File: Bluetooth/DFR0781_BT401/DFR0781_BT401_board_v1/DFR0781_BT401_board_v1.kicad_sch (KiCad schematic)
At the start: 8 parts, among them J1 PINHD_1x8_Female, J2 PINHD_1x6_Male

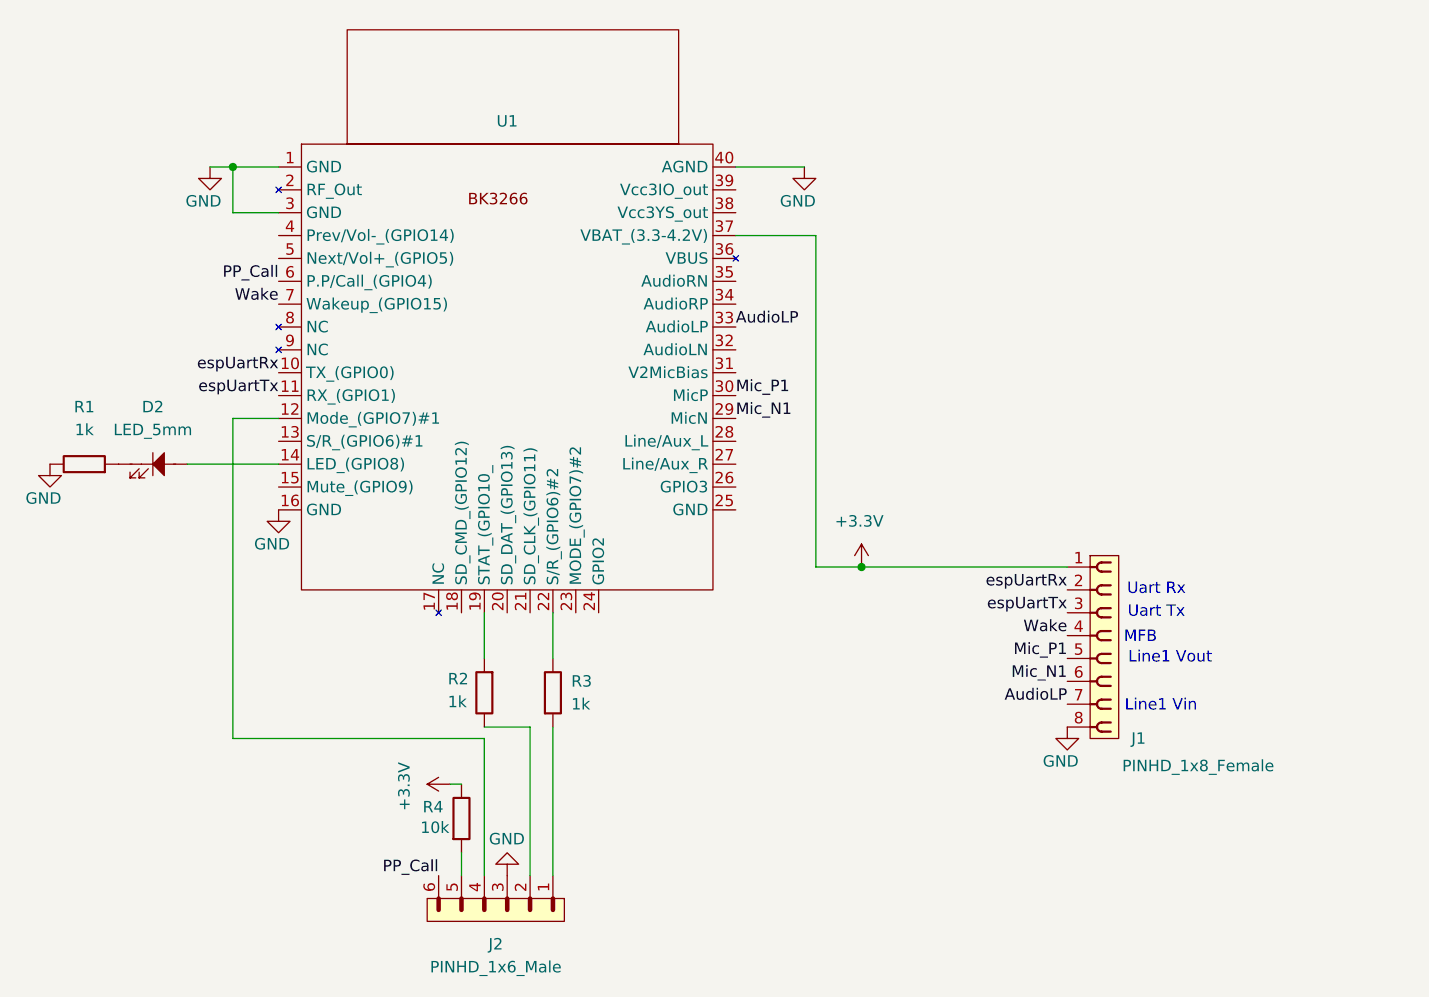
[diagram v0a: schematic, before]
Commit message: BT401 notes: measured round-pad connections (GND, SGND via 10 ohm, 5V=VCC, TX, RX)
Co-Authored-By: Claude Opus 5.5 <noreply@anthropic.com>
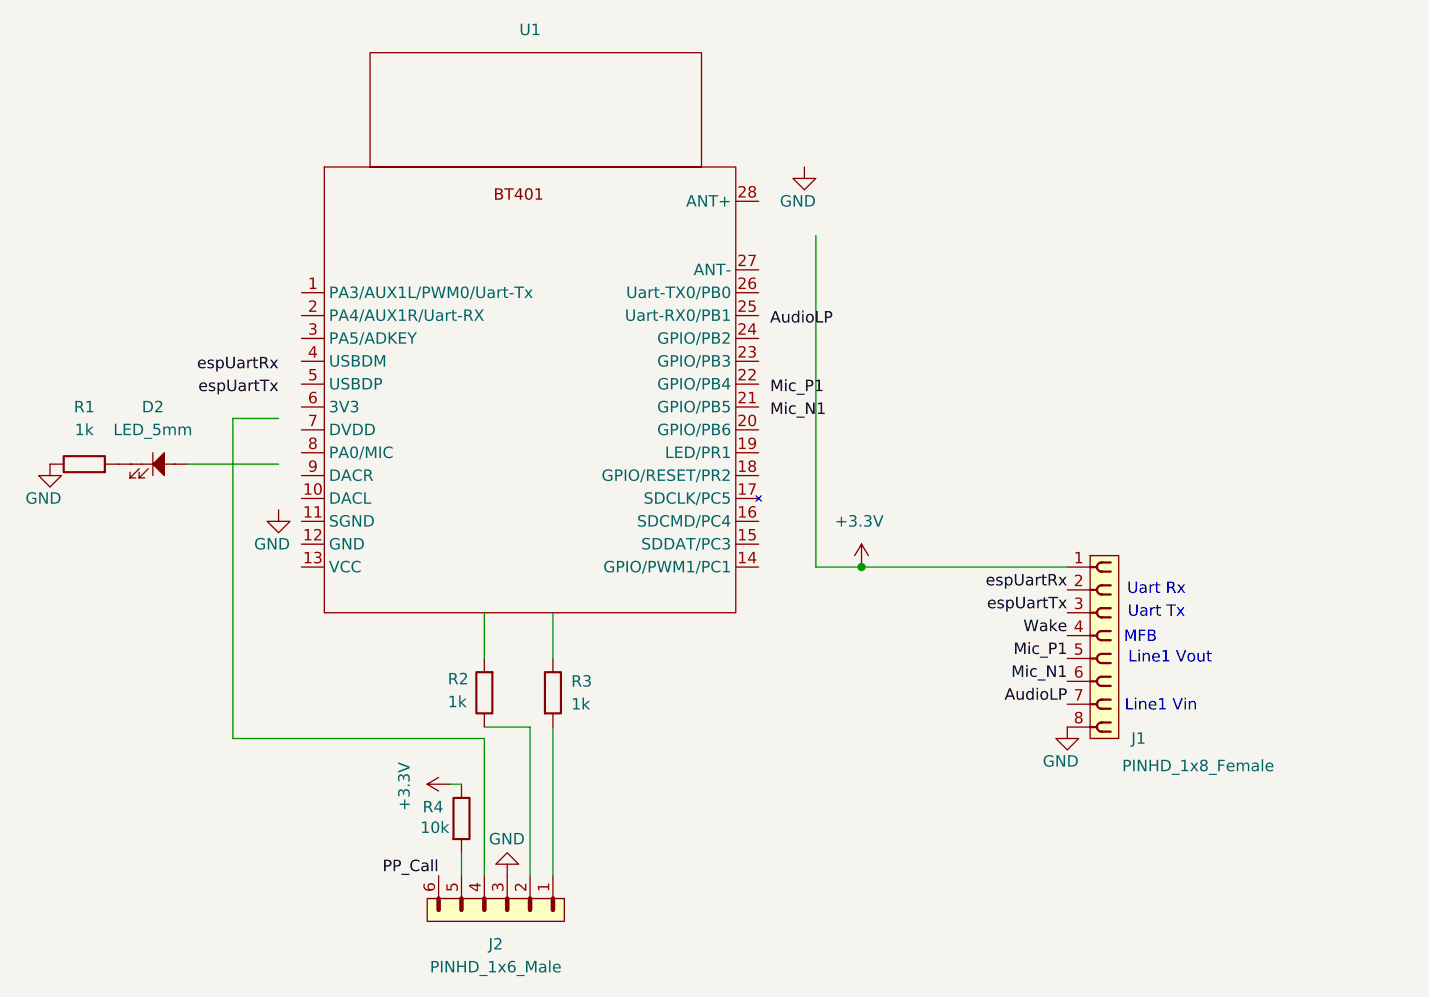
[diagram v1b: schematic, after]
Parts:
- removed U1: (no value), Custom:BK3266SR, symbol Custom:BK3266SR
- added U1: (no value), Custom:DFR0781_BT401, symbol Custom:DFR0781_BT401_Bluetooth_Module

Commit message: BT401 adapter: new symbol and footprint (round pads joined to edge pads)
Co-Authored-By: Claude Opus 5.5 <noreply@anthropic.com>
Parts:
- U1: footprint Custom:DFR0781_BT401 -> Custom:DFR0781_BT401_new
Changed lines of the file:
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@@
 			)
 		)
-		(property "Footprint" "Custom:DFR0781_BT401"
+		(property "Footprint" "Custom:DFR0781_BT401_new"
 			(at 94.742 74.168 0)
 			(hide yes)
@@
 			)
 		)
-		(property "Datasheet" ""
+		(property "Datasheet" "https://github.com/DFRobot/DFRobot_BT401"
 			(at 77.47 72.39 0)
 			(hide yes)

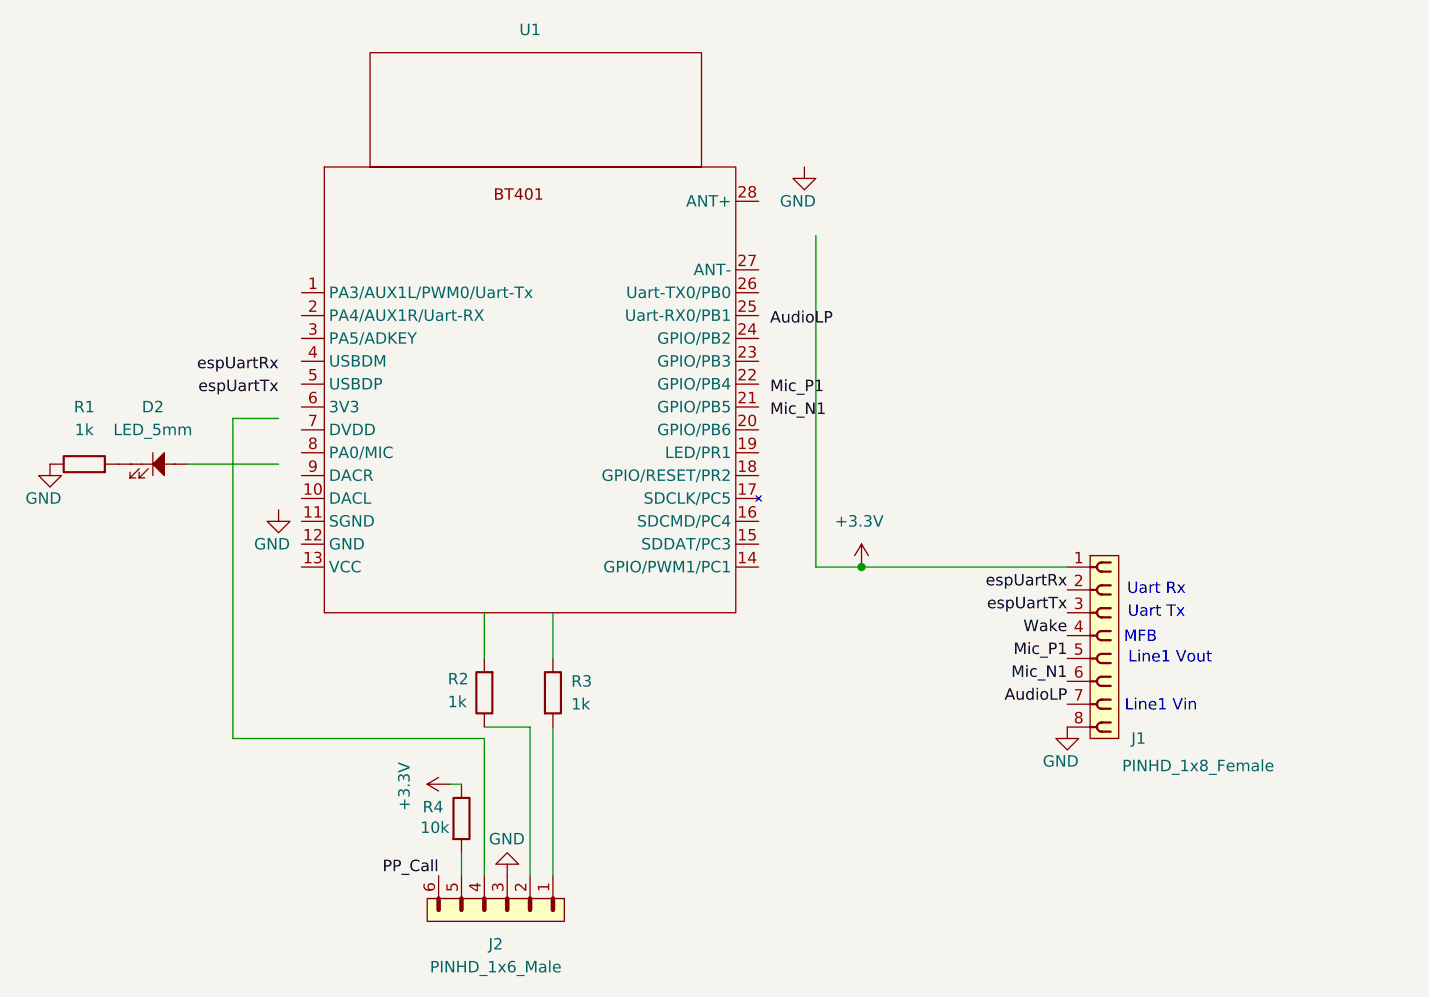
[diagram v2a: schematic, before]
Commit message: BT401: Bluetooth on/off switch puts the module in idle mode (7 mA); re-send DAC off after a module restart
Co-Authored-By: Claude Opus 5.5 <noreply@anthropic.com>
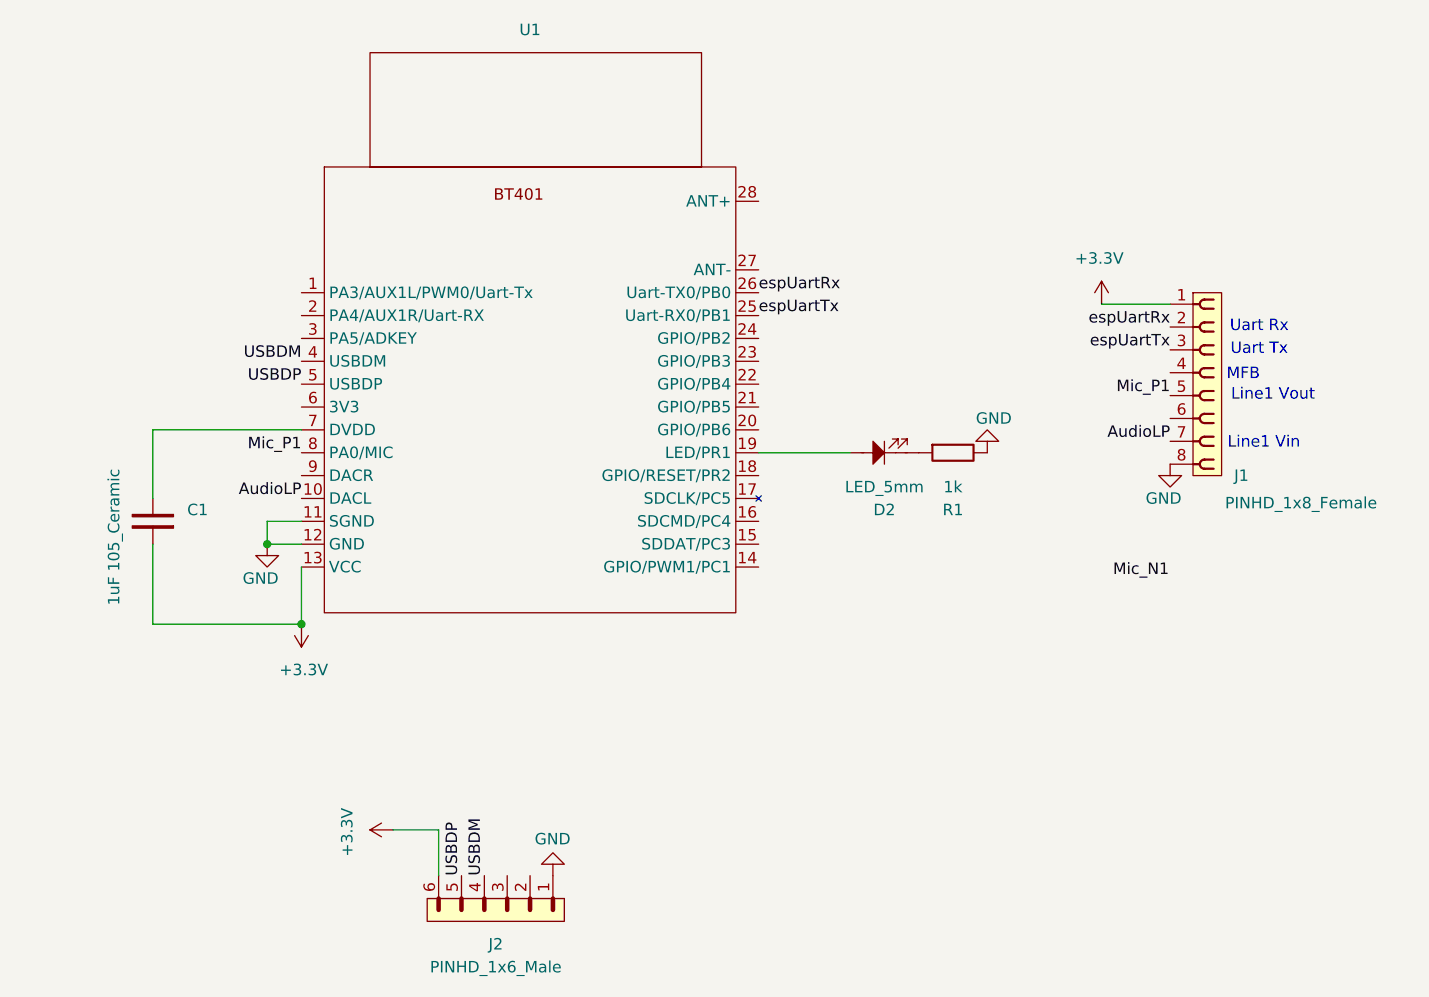
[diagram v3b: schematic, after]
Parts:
- removed R2, R3: 1k, Resistor_THT:R_Axial_DIN0207_L6.3mm_D2.5mm_P10.16mm_Horizontal, symbol PCM_SL_Resistors:1k
- removed R4: 10k, Resistor_THT:R_Axial_DIN0207_L6.3mm_D2.5mm_P10.16mm_Horizontal, symbol PCM_SL_Resistors:1k
- added C1: 1uF 105_Ceramic, Capacitor_THT:C_Disc_D5.0mm_W2.5mm_P2.50mm, symbol PCM_SL_Capacitors:104_Ceramic
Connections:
- net PP_Call is gone; now on net +3.3V: J2.6
- net +3.3V: now also U1.13 (VCC), C1.2
- net AudioLP: now also U1.10 (DACL)
- net GND: now also J2.1, U1.11 (SGND), U1.12 (GND); no longer J2.3
- net Mic_N1: no longer J1.6
- net Mic_P1: now also U1.8 (PA0/MIC)
- net espUartRx: now also U1.26 (Uart-TX0/PB0)
- net espUartTx: now also U1.25 (Uart-RX0/PB1)
- net at U1.19 (LED/PR1): now also D2.2
- net USBDM: now reaches U1.4 (USBDM)
- net USBDM: now also J2.4
- net USBDP: now reaches U1.5 (USBDP)
- net USBDP: now also J2.5
- net at U1.7 (DVDD): now also C1.1
- net Wake: no longer names the net of J1.4
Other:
- moved on the sheet: D2, J1, R1

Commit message: BT401 adapter board v1 released for fab (C1 to GND, reset and DACR on J2); docs: designed, not yet built or tested
Co-Authored-By: Claude Opus 5.5 <noreply@anthropic.com>
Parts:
- renumbered D2 to D1
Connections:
- net +3.3V: no longer C1.2
- net GND: now also C1.2
- net Reset: now reaches U1.18 (GPIO/RESET/PR2)
- net Reset: now also J2.2
- net AudioRP: now reaches U1.9 (DACR)
- net AudioRP: now also J2.3
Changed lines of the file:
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@@
-	)
-	(junction
-		(at 72.39 119.38)
-		(diameter 0)
-		(color 0 0 0 0)
 	)
 	(junction
@@
 	(wire
 		(pts
+			(xy 123.19 102.87) (xy 127 102.87)
+		)
+		(stroke
+			(width 0)
+			(type default)
+		)
+	)
+	(wire
+		(pts
 			(xy 133.35 100.33) (xy 123.19 100.33)
 		)
@@
 	(wire
 		(pts
+			(xy 97.79 135.89) (xy 97.79 147.32)
+		)
+		(stroke
+			(width 0)
+			(type default)
+		)
+	)
+	(wire
+		(pts
 			(xy 82.55 142.24) (xy 87.63 142.24)
 		)
@@
 	(wire
 		(pts
-			(xy 55.88 110.49) (xy 55.88 119.38)
+			(xy 55.88 110.49) (xy 68.58 110.49)
 		)
 		(stroke
@@
 	(wire
 		(pts
+			(xy 127 135.89) (xy 97.79 135.89)
+		)
+		(stroke
+			(width 0)
+			(type default)
+		)
+	)
+	(wire
+		(pts
 			(xy 72.39 97.79) (xy 55.88 97.79)
 		)
@@
 	(wire
 		(pts
-			(xy 55.88 119.38) (xy 72.39 119.38)
-		)
-		(stroke
-			(width 0)
-			(type default)
-		)
-	)
-	(wire
-		(pts
 			(xy 168.91 83.82) (xy 161.29 83.82)
 		)
@@
 		)
 	)
-	(label "Mic_N1"
-		(at 162.56 114.3 0)
-		(effects
-			(font
-				(size 1.27 1.27)
-			)
-			(justify left bottom)
+	(wire
+		(pts
+			(xy 127 102.87) (xy 127 135.89)
+		)
+		(stroke
+			(width 0)
+			(type default)
 		)
 	)
@@
 		)
 	)
+	(label "AudioRP"
+		(at 72.39 102.87 180)
+		(effects
+			(font
+				(size 1.27 1.27)
+			)
+			(justify right bottom)
+		)
+	)
 	(label "USBDP"
 		(at 90.17 147.32 90)
@@
 		)
 	)
+	(label "Reset"
+		(at 99.06 135.89 0)
+		(effects
+			(font
+				(size 1.27 1.27)
+			)
+			(justify left bottom)
+		)
+	)
 	(label "USBDM"
 		(at 92.71 147.32 90)
+		(effects
+			(font
+				(size 1.27 1.27)
+			)
+			(justify left bottom)
+		)
+	)
+	(label "AudioRP"
+		(at 95.25 147.32 90)
 		(effects
 			(font
@@
 		(in_pos_files yes)
 		(dnp no)
-		(property "Reference" "#PWR046"
+		(property "Reference" "#PWR05"
 			(at 148.59 93.98 0)
 			(hide yes)
@@
 			(project "DFR0781_BT401_board_v1"
 				(path "/ae5d8edc-3faa-41fe-90b3-432a5a2c7d06"
-					(reference "#PWR046")
+					(reference "#PWR05")
 					(unit 1)
 				)
@@
 		(in_pos_files yes)
 		(dnp no)
-		(property "Reference" "#PWR044"
+		(property "Reference" "#PWR06"
 			(at 161.29 87.63 0)
 			(hide yes)
@@
 			(project "DFR0781_BT401_board_v1"
 				(path "/ae5d8edc-3faa-41fe-90b3-432a5a2c7d06"
-					(reference "#PWR044")
+					(reference "#PWR06")
 					(unit 1)
 				)
@@
 		(in_pos_files yes)
 		(dnp no)
-		(property "Reference" "#PWR042"
+		(property "Reference" "#PWR01"
 			(at 68.58 116.84 0)
 			(hide yes)
@@
 			(project "DFR0781_BT401_board_v1"
 				(path "/ae5d8edc-3faa-41fe-90b3-432a5a2c7d06"
-					(reference "#PWR042")
+					(reference "#PWR01")
 					(unit 1)
 				)
@@
 		(in_pos_files yes)
 		(dnp no)
-		(property "Reference" "#PWR047"
+		(property "Reference" "#PWR04"
 			(at 100.33 140.97 0)
 			(hide yes)
@@
 			(project "DFR0781_BT401_board_v1"
 				(path "/ae5d8edc-3faa-41fe-90b3-432a5a2c7d06"
-					(reference "#PWR047")
+					(reference "#PWR04")
 					(unit 1)
 				)
@@
 		(in_pos_files yes)
 		(dnp no)
-		(property "Reference" "#PWR049"
+		(property "Reference" "#PWR03"
 			(at 86.36 142.24 0)
 			(hide yes)
@@
 			(project "DFR0781_BT401_board_v1"
 				(path "/ae5d8edc-3faa-41fe-90b3-432a5a2c7d06"
-					(reference "#PWR049")
+					(reference "#PWR03")
 					(unit 1)
 				)
@@
 		(in_pos_files yes)
 		(dnp no)
-		(property "Reference" "#PWR045"
+		(property "Reference" "#PWR02"
 			(at 72.39 115.57 0)
 			(hide yes)
@@
 			(project "DFR0781_BT401_board_v1"
 				(path "/ae5d8edc-3faa-41fe-90b3-432a5a2c7d06"
-					(reference "#PWR045")
+					(reference "#PWR02")
 					(unit 1)
 				)
@@
 		(in_pos_files yes)
 		(dnp no)
-		(property "Reference" "#PWR048"
+		(property "Reference" "#PWR07"
 			(at 168.91 107.95 0)
 			(hide yes)
@@
 			(project "DFR0781_BT401_board_v1"
 				(path "/ae5d8edc-3faa-41fe-90b3-432a5a2c7d06"
-					(reference "#PWR048")
+					(reference "#PWR07")
 					(unit 1)
 				)
@@
 		(dnp no)
 		(fields_autoplaced yes)
-		(property "Reference" "D2"
+		(property "Reference" "D1"
 			(at 137.16 106.68 0)
 			(show_name no)
@@
 			(project "DFR0781_BT401_board_v1"
 				(path "/ae5d8edc-3faa-41fe-90b3-432a5a2c7d06"
-					(reference "D2")
+					(reference "D1")
 					(unit 1)
 				)
